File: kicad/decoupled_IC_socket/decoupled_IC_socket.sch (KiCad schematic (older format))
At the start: 4 parts

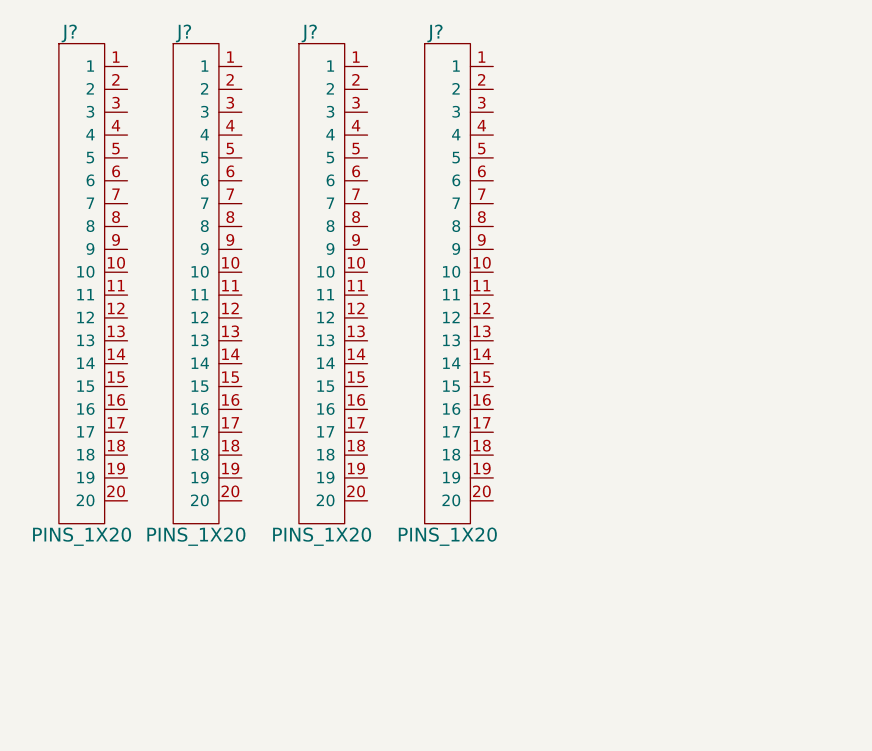
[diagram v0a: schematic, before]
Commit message: * decoupled IC socket finished
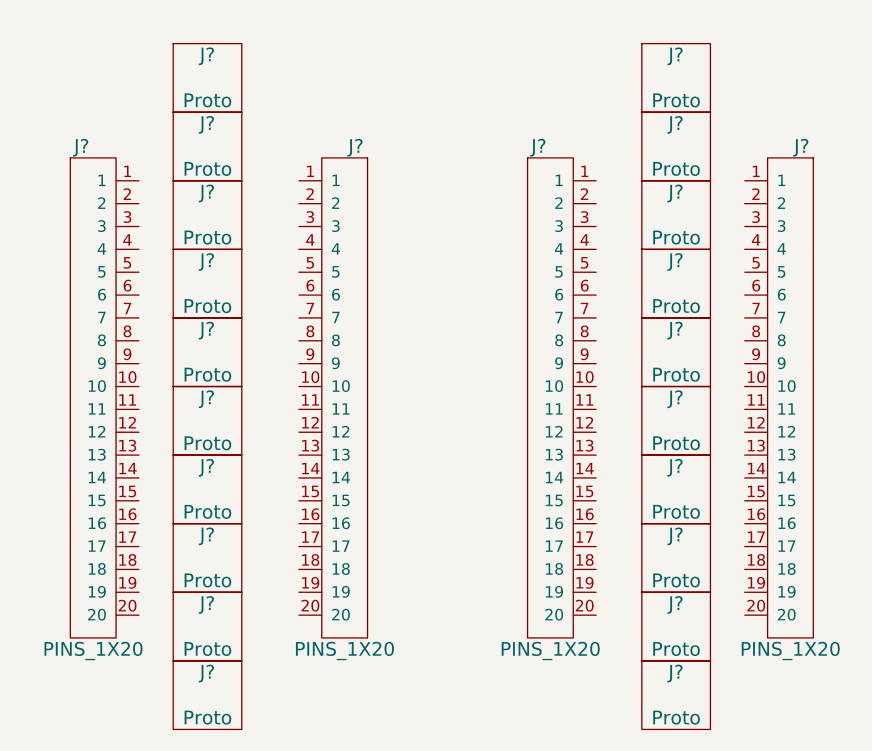
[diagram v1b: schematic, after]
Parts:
- added J? (x20): Proto, SquantorProto:proto-0254-02X02-P020, symbol Proto
- J? (x4): footprint (none) -> SquantorConnectors:Header-0254-1X20-H015
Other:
- moved on the sheet: J?

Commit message: * finished decoupled IC socket PCB
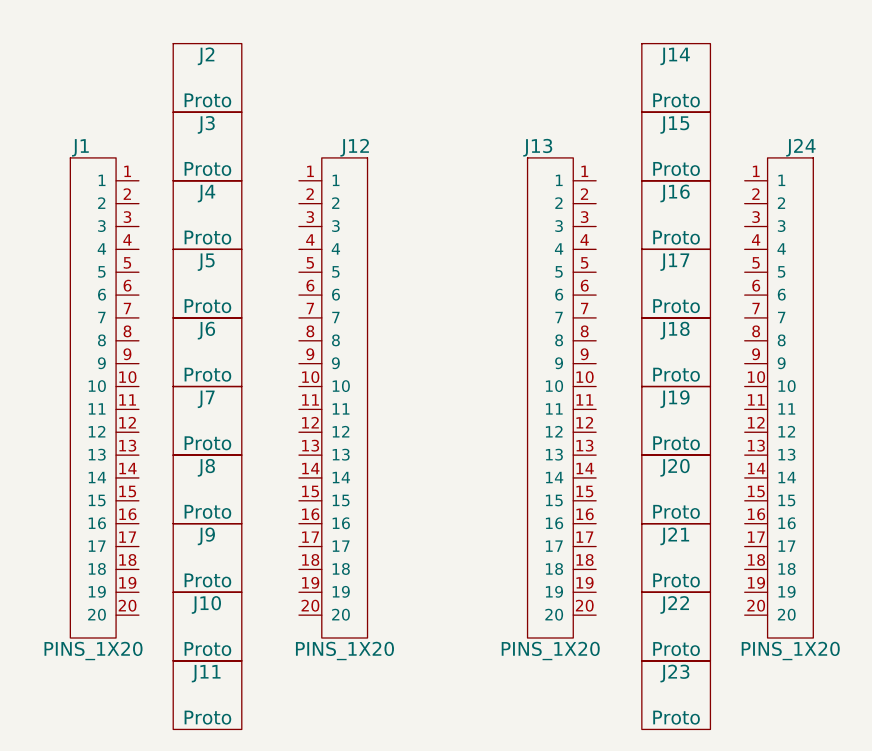
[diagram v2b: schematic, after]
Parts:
- gave numbers to parts that had none: 24
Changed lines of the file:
@@
 $EndDescr
 $Comp
-L PINS_1X20 J?
+L PINS_1X20 J1
 U 1 1 59BAD962
 P 850 2250
-F 0 "J?" H 800 3350 60  0000 C CNN
+F 0 "J1" H 800 3350 60  0000 C CNN
 F 1 "PINS_1X20" H 850 1150 60  0000 C CNN
 F 2 "SquantorConnectors:Header-0254-1X20-H015" H 850 3200 60  0001 C CNN
@@
 $EndComp
 $Comp
-L PINS_1X20 J?
+L PINS_1X20 J12
 U 1 1 59BADA31
 P 1950 2250
-F 0 "J?" H 1900 3350 60  0000 C CNN
+F 0 "J12" H 1900 3350 60  0000 C CNN
 F 1 "PINS_1X20" H 1950 1150 60  0000 C CNN
 F 2 "SquantorConnectors:Header-0254-1X20-H015" H 1950 3200 60  0001 C CNN
@@
 $EndComp
 $Comp
-L PINS_1X20 J?
+L PINS_1X20 J13
 U 1 1 59BADAA0
 P 2850 2250
-F 0 "J?" H 2800 3350 60  0000 C CNN
+F 0 "J13" H 2800 3350 60  0000 C CNN
 F 1 "PINS_1X20" H 2850 1150 60  0000 C CNN
 F 2 "SquantorConnectors:Header-0254-1X20-H015" H 2850 3200 60  0001 C CNN
@@
 $EndComp
 $Comp
-L PINS_1X20 J?
+L PINS_1X20 J24
 U 1 1 59BADAF1
 P 3900 2250
-F 0 "J?" H 3850 3350 60  0000 C CNN
+F 0 "J24" H 3850 3350 60  0000 C CNN
 F 1 "PINS_1X20" H 3900 1150 60  0000 C CNN
 F 2 "SquantorConnectors:Header-0254-1X20-H015" H 3900 3200 60  0001 C CNN
@@
 $EndComp
 $Comp
-L Proto J?
+L Proto J7
 U 1 1 59BAE168
 P 1350 2350
-F 0 "J?" H 1350 2450 60  0000 C CNN
+F 0 "J7" H 1350 2450 60  0000 C CNN
 F 1 "Proto" H 1350 2250 60  0000 C CNN
 F 2 "SquantorProto:proto-0254-02X02-P020" H 1350 2350 60  0001 C CNN
@@
 $EndComp
 $Comp
-L Proto J?
+L Proto J8
 U 1 1 59BAE259
 P 1350 2650
-F 0 "J?" H 1350 2750 60  0000 C CNN
+F 0 "J8" H 1350 2750 60  0000 C CNN
 F 1 "Proto" H 1350 2550 60  0000 C CNN
 F 2 "SquantorProto:proto-0254-02X02-P020" H 1350 2650 60  0001 C CNN
@@
 $EndComp
 $Comp
-L Proto J?
+L Proto J9
 U 1 1 59BAE5DC
 P 1350 2950
-F 0 "J?" H 1350 3050 60  0000 C CNN
+F 0 "J9" H 1350 3050 60  0000 C CNN
 F 1 "Proto" H 1350 2850 60  0000 C CNN
 F 2 "SquantorProto:proto-0254-02X02-P020" H 1350 2950 60  0001 C CNN
@@
 $EndComp
 $Comp
-L Proto J?
+L Proto J10
 U 1 1 59BAE611
 P 1350 3250
-F 0 "J?" H 1350 3350 60  0000 C CNN
+F 0 "J10" H 1350 3350 60  0000 C CNN
 F 1 "Proto" H 1350 3150 60  0000 C CNN
 F 2 "SquantorProto:proto-0254-02X02-P020" H 1350 3250 60  0001 C CNN
@@
 $EndComp
 $Comp
-L Proto J?
+L Proto J11
 U 1 1 59BAE661
 P 1350 3550
-F 0 "J?" H 1350 3650 60  0000 C CNN
+F 0 "J11" H 1350 3650 60  0000 C CNN
 F 1 "Proto" H 1350 3450 60  0000 C CNN
 F 2 "SquantorProto:proto-0254-02X02-P020" H 1350 3550 60  0001 C CNN
@@
 $EndComp
 $Comp
-L Proto J?
+L Proto J2
 U 1 1 59BAEA07
 P 1350 850
-F 0 "J?" H 1350 950 60  0000 C CNN
+F 0 "J2" H 1350 950 60  0000 C CNN
 F 1 "Proto" H 1350 750 60  0000 C CNN
 F 2 "SquantorProto:proto-0254-02X02-P020" H 1350 850 60  0001 C CNN
@@
 $EndComp
 $Comp
-L Proto J?
+L Proto J3
 U 1 1 59BAEA0D
 P 1350 1150
-F 0 "J?" H 1350 1250 60  0000 C CNN
+F 0 "J3" H 1350 1250 60  0000 C CNN
 F 1 "Proto" H 1350 1050 60  0000 C CNN
 F 2 "SquantorProto:proto-0254-02X02-P020" H 1350 1150 60  0001 C CNN
@@
 $EndComp
 $Comp
-L Proto J?
+L Proto J4
 U 1 1 59BAEA13
 P 1350 1450
-F 0 "J?" H 1350 1550 60  0000 C CNN
+F 0 "J4" H 1350 1550 60  0000 C CNN
 F 1 "Proto" H 1350 1350 60  0000 C CNN
 F 2 "SquantorProto:proto-0254-02X02-P020" H 1350 1450 60  0001 C CNN
@@
 $EndComp
 $Comp
-L Proto J?
+L Proto J5
 U 1 1 59BAEA19
 P 1350 1750
-F 0 "J?" H 1350 1850 60  0000 C CNN
+F 0 "J5" H 1350 1850 60  0000 C CNN
 F 1 "Proto" H 1350 1650 60  0000 C CNN
 F 2 "SquantorProto:proto-0254-02X02-P020" H 1350 1750 60  0001 C CNN
@@
 $EndComp
 $Comp
-L Proto J?
+L Proto J6
 U 1 1 59BAEA1F
 P 1350 2050
-F 0 "J?" H 1350 2150 60  0000 C CNN
+F 0 "J6" H 1350 2150 60  0000 C CNN
 F 1 "Proto" H 1350 1950 60  0000 C CNN
 F 2 "SquantorProto:proto-0254-02X02-P020" H 1350 2050 60  0001 C CNN
@@
 $EndComp
 $Comp
-L Proto J?
+L Proto J19
 U 1 1 59BAF1B6
 P 3400 2350
-F 0 "J?" H 3400 2450 60  0000 C CNN
+F 0 "J19" H 3400 2450 60  0000 C CNN
 F 1 "Proto" H 3400 2250 60  0000 C CNN
 F 2 "SquantorProto:proto-0254-02X02-P020" H 3400 2350 60  0001 C CNN
@@
 $EndComp
 $Comp
-L Proto J?
+L Proto J20
 U 1 1 59BAF1BC
 P 3400 2650
-F 0 "J?" H 3400 2750 60  0000 C CNN
+F 0 "J20" H 3400 2750 60  0000 C CNN
 F 1 "Proto" H 3400 2550 60  0000 C CNN
 F 2 "SquantorProto:proto-0254-02X02-P020" H 3400 2650 60  0001 C CNN
@@
 $EndComp
 $Comp
-L Proto J?
+L Proto J21
 U 1 1 59BAF1C2
 P 3400 2950
-F 0 "J?" H 3400 3050 60  0000 C CNN
+F 0 "J21" H 3400 3050 60  0000 C CNN
 F 1 "Proto" H 3400 2850 60  0000 C CNN
 F 2 "SquantorProto:proto-0254-02X02-P020" H 3400 2950 60  0001 C CNN
@@
 $EndComp
 $Comp
-L Proto J?
+L Proto J22
 U 1 1 59BAF1C8
 P 3400 3250
-F 0 "J?" H 3400 3350 60  0000 C CNN
+F 0 "J22" H 3400 3350 60  0000 C CNN
 F 1 "Proto" H 3400 3150 60  0000 C CNN
 F 2 "SquantorProto:proto-0254-02X02-P020" H 3400 3250 60  0001 C CNN
@@
 $EndComp
 $Comp
-L Proto J?
+L Proto J23
 U 1 1 59BAF1CE
 P 3400 3550
-F 0 "J?" H 3400 3650 60  0000 C CNN
+F 0 "J23" H 3400 3650 60  0000 C CNN
 F 1 "Proto" H 3400 3450 60  0000 C CNN
 F 2 "SquantorProto:proto-0254-02X02-P020" H 3400 3550 60  0001 C CNN
@@
 $EndComp
 $Comp
-L Proto J?
+L Proto J14
 U 1 1 59BAF1D4
 P 3400 850
-F 0 "J?" H 3400 950 60  0000 C CNN
+F 0 "J14" H 3400 950 60  0000 C CNN
 F 1 "Proto" H 3400 750 60  0000 C CNN
 F 2 "SquantorProto:proto-0254-02X02-P020" H 3400 850 60  0001 C CNN
@@
 $EndComp
 $Comp
-L Proto J?
+L Proto J15
 U 1 1 59BAF1DA
 P 3400 1150
-F 0 "J?" H 3400 1250 60  0000 C CNN
+F 0 "J15" H 3400 1250 60  0000 C CNN
 F 1 "Proto" H 3400 1050 60  0000 C CNN
 F 2 "SquantorProto:proto-0254-02X02-P020" H 3400 1150 60  0001 C CNN
@@
 $EndComp
 $Comp
-L Proto J?
+L Proto J16
 U 1 1 59BAF1E0
 P 3400 1450
-F 0 "J?" H 3400 1550 60  0000 C CNN
+F 0 "J16" H 3400 1550 60  0000 C CNN
 F 1 "Proto" H 3400 1350 60  0000 C CNN
 F 2 "SquantorProto:proto-0254-02X02-P020" H 3400 1450 60  0001 C CNN
@@
 $EndComp
 $Comp
-L Proto J?
+L Proto J17
 U 1 1 59BAF1E6
 P 3400 1750
-F 0 "J?" H 3400 1850 60  0000 C CNN
+F 0 "J17" H 3400 1850 60  0000 C CNN
 F 1 "Proto" H 3400 1650 60  0000 C CNN
 F 2 "SquantorProto:proto-0254-02X02-P020" H 3400 1750 60  0001 C CNN
@@
 $EndComp
 $Comp
-L Proto J?
+L Proto J18
 U 1 1 59BAF1EC
 P 3400 2050
-F 0 "J?" H 3400 2150 60  0000 C CNN
+F 0 "J18" H 3400 2150 60  0000 C CNN
 F 1 "Proto" H 3400 1950 60  0000 C CNN
 F 2 "SquantorProto:proto-0254-02X02-P020" H 3400 2050 60  0001 C CNN
